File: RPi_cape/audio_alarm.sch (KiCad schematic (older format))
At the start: 70 parts, among them J13 Conn_01x02, J14 Conn_01x02, Q11 MMBT3904, Q12 MMBT3906, Q13 MMBT3904, Q5 MMBT3904, Q6 DNP, Q7 DNP, Q8 MMBT3904, U24 TL431A, U25 LM2903, U26 MIC1557, U27 MIC1557, U28 LM4871M

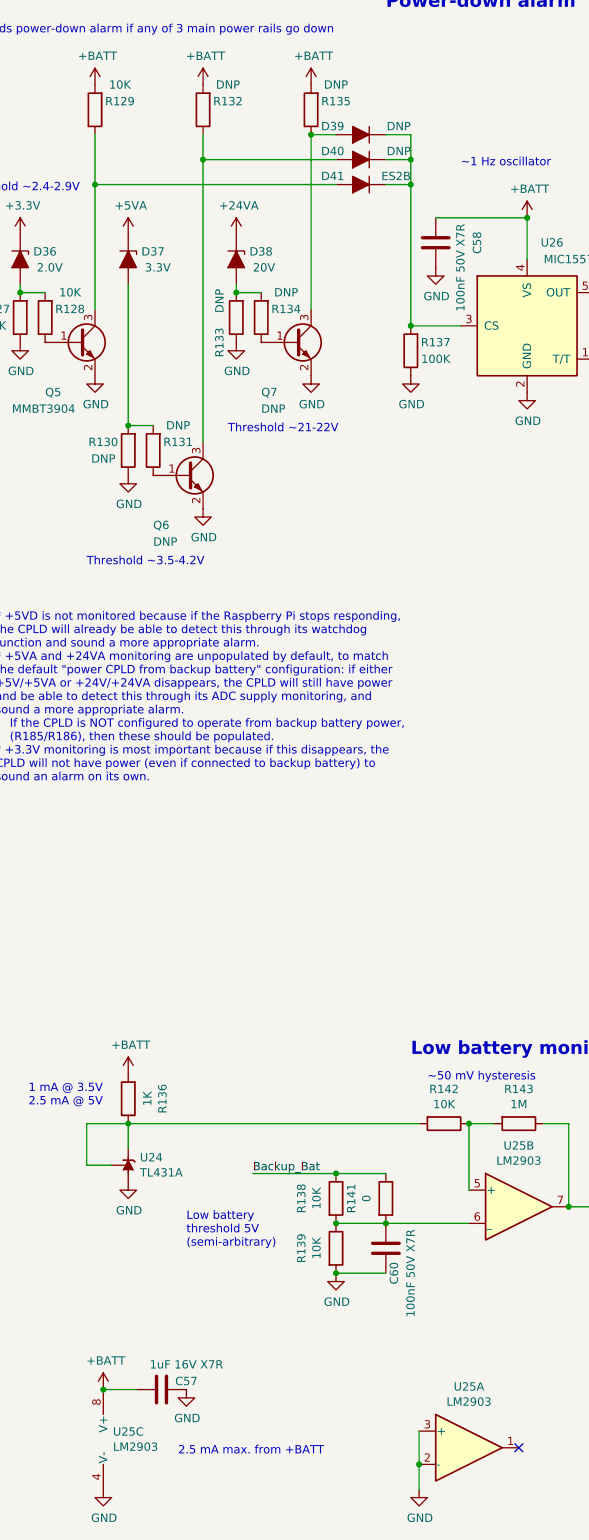
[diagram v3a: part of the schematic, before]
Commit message: Better valve monitoring, finalized layout and manufacturing files
Created assembly and fabrication drawings, assigned all BOM parts, generally made design ready for ordering
Added strain-relief slots and barb mounting dimensions for digital pressure sensors
Changed valve drivers from discrete power MOSFETs to "smart" industrial/automotive driver ICs for the current monitoring, including valve-movement monitor for #4
Connected RPi_Valve* signals to larger CPLD footprint, changed Raspberry Pi pin assignment as a result to ease PCB routing
Updated footprints, page layout to create readable assembly drawing
Added current-measurement testpoints for CPLD power from BATT+
Changed power diodes in power-down-alarm circuit to small-signal parts for more compact layout
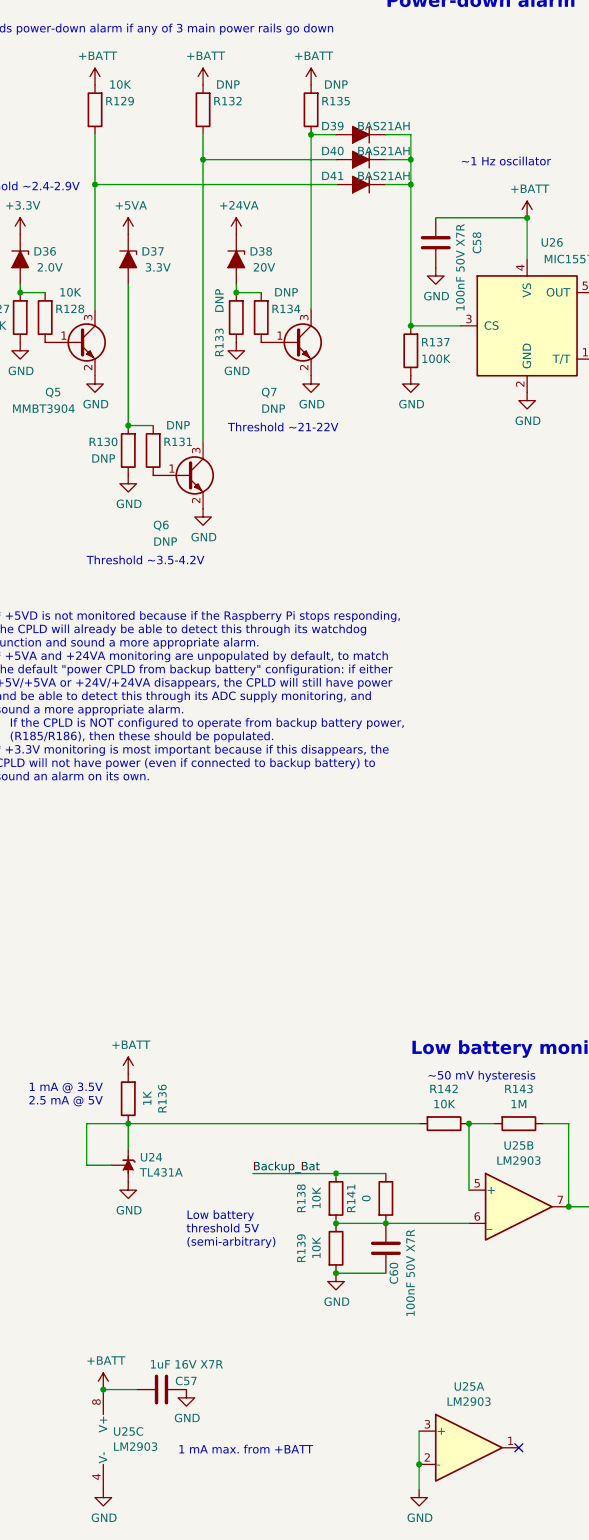
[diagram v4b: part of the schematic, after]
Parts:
- D36: footprint Diode_SMD:D_SOD-123 -> Ventilator:D_SOD-123; Manufacturer (none) -> ON Semiconductor; Part Number (none) -> MMSZ4679T1G
- D37, D52: footprint Diode_SMD:D_SOD-123 -> Ventilator:D_SOD-123; Manufacturer (none) -> ON Semiconductor; Part Number (none) -> MMSZ4684T1G
- D38: footprint Diode_SMD:D_SOD-123 -> Ventilator:D_SOD-123; Manufacturer (none) -> ON Semiconductor; Part Number (none) -> MMSZ4707T1G
- D39, D40: value DNP -> BAS21AH; footprint Diode_SMD:D_SMA -> Ventilator:D_SOD-323; Manufacturer Vishay -> ON Semiconductor; Part Number ES2G-E3/52T -> BAS21AHT1G
- D41: value ES2B -> BAS21AH; footprint Diode_SMD:D_SMA -> Ventilator:D_SOD-323; Manufacturer Vishay -> ON Semiconductor; Part Number ES2G-E3/52T -> BAS21AHT1G
- D42, D43: footprint Diode_SMD:D_SMA -> Ventilator:D_SMA
- Q11, Q13, Q5, Q8: footprint Package_TO_SOT_SMD:SOT-23 -> Ventilator:SOT-23; Manufacturer (none) -> Diodes Inc.; Part Number (none) -> MMBT3904-7-F
- Q12: footprint Package_TO_SOT_SMD:SOT-23 -> Ventilator:SOT-23; Manufacturer (none) -> Nexperia; Part Number (none) -> MMBT3906,215
- Q6, Q7, U24: footprint Package_TO_SOT_SMD:SOT-23 -> Ventilator:SOT-23
- R127, R128, R129, R138, R139, R142, R146, R148, R151, R187, R188, R191: Manufacturer (none) -> KOA Speer; Part Number (none) -> RK73H2BTTD1002F
- R136, R147: Manufacturer (none) -> KOA Speer; Part Number (none) -> RK73H2BTTD1001F
- R137, R149, R150: Manufacturer (none) -> KOA Speer; Part Number (none) -> RK73H2BTTD1003F
- R140, R143: Manufacturer (none) -> KOA Speer; Part Number (none) -> RK73H2BTTD1004F
- R141, R177, R178: Manufacturer (none) -> Panasonic; Part Number (none) -> ERJ-8GEY0R00V
- R144: Manufacturer (none) -> KOA Speer; Part Number (none) -> RK73H2BTTD2703F
- R190: Manufacturer (none) -> KOA Speer; Part Number (none) -> RK73H2BTTD3001F
- U25: footprint Package_SO:VSSOP-8_3.0x3.0mm_P0.65mm -> Ventilator:VSSOP-8_3.0x3.0mm_P0.65mm
- U26, U27: footprint Package_TO_SOT_SMD:SOT-23-5 -> Ventilator:SOT-23-5
- U28: footprint Package_SO:SOIC-8_3.9x4.9mm_P1.27mm -> Ventilator:SOIC-8_3.9x4.9mm_P1.27mm
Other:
- note added: "1 mA max. from +BATT"
- note removed: "2.5 mA max. from +BATT"

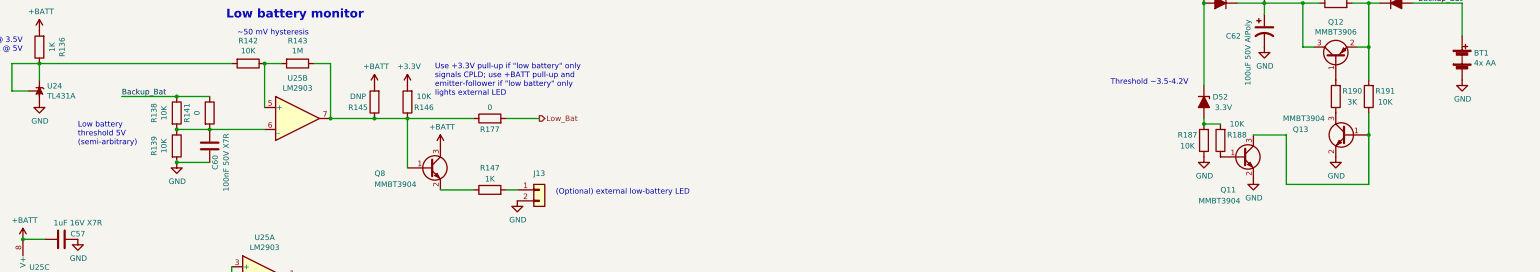
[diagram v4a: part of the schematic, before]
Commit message: Manufacturing clean-up
Corrections and additions to BOM etc. for manufacturing
Added power draw tracking spreadsheet
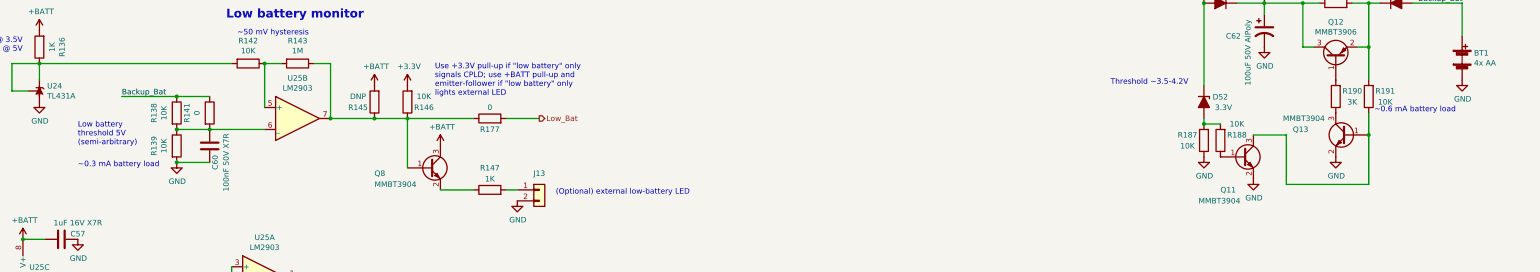
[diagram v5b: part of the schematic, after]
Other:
- note added: "~~0.3 mA battery load"
- note added: "~~0.6 mA battery load"
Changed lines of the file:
@@
 	1    0    0    -1
 $EndComp
+Text Notes 13650 8000 0    50   ~ 0
+~~0.6 mA battery load
+Text Notes 1850 8500 0    50   ~ 0
+~~0.3 mA battery load
 $EndSCHEMATC

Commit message: Safety additions
Switched CPLD_ADC7 to +24V monitoring (from +5V monitoring), and added CPLD ~Bat_On digital input(s) to know when it's running from backup battery, to cover low-input-voltage edge cases
Added series 1K resistors (R226-231) on CPLD<->RPi Comms1-6 lines, to protect CPLD in case of overvoltage from RPi failure
Added optional input TVS D23 to handle sustained over-voltage or large surges
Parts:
- added D14, D22: BAS21AH, Ventilator:D_SOD-323, symbol Device:D_ALT
- added R224, R225: 10K, Resistor_SMD:R_1206_3216Metric, symbol Device:R
- D37: value 3.3V -> DNP (3.3V)
- D38: value 20V -> DNP (20V)
- D39: value BAS21AH -> DNP (BAS21AH)
- Q6: value DNP -> MMBT3904; Manufacturer (none) -> Diodes Inc.; Part Number (none) -> MMBT3904-7-F
- R130: value DNP -> 1K; Manufacturer (none) -> KOA Speer; Part Number (none) -> RK73H2BTTD1001F
- R131, R132: value DNP -> 10K; Manufacturer (none) -> KOA Speer; Part Number (none) -> RK73H2BTTD1002F
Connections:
- net +3V3: now also R225.2
- net at Q12.1 (B), R190.2: now also R224.1
- net at D43.1 (K), Q12.2 (E), R189.2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: now also R224.2
- net at Q13.3 (C), R190.1: now also D22.1 (K)
- net at D37.2 (A), R130.2, R131.2: now also D14.1 (K)
- new net +1V8: D14.2 (A)
- new net ~Bat_On: D22.2 (A), R225.1
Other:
- note added: "Can monitor either +5VA or +1.8V,\ndepending on which diode is populated\n+5VA: threshold ~~3.5-4.2V, R130=10K (for 50uA Izener nom.)\n+1.8V: threshold ~~0.9-1.4V, R130=1K (for 0.5mA Idiode nom.)"
- note added: "Signal to CPLD, goes low when\nrunning from backup battery\npower"
- moved on the sheet: BT1, D43, R191

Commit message: Docs cleanup
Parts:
- C65: Part Number GCM32EC71H106KA03 -> GCM32EC71H106KA03L
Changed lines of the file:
@@
 F 3 "~" H 7700 1500 50  0001 C CNN
 F 4 "Murata" H 7700 1500 50  0001 C CNN "Manufacturer"
-F 5 "GCM32EC71H106KA03" H 7700 1500 50  0001 C CNN "Part Number"
+F 5 "GCM32EC71H106KA03L" H 7700 1500 50  0001 C CNN "Part Number"
 	1    7700 1500
 	-1   0    0    -1

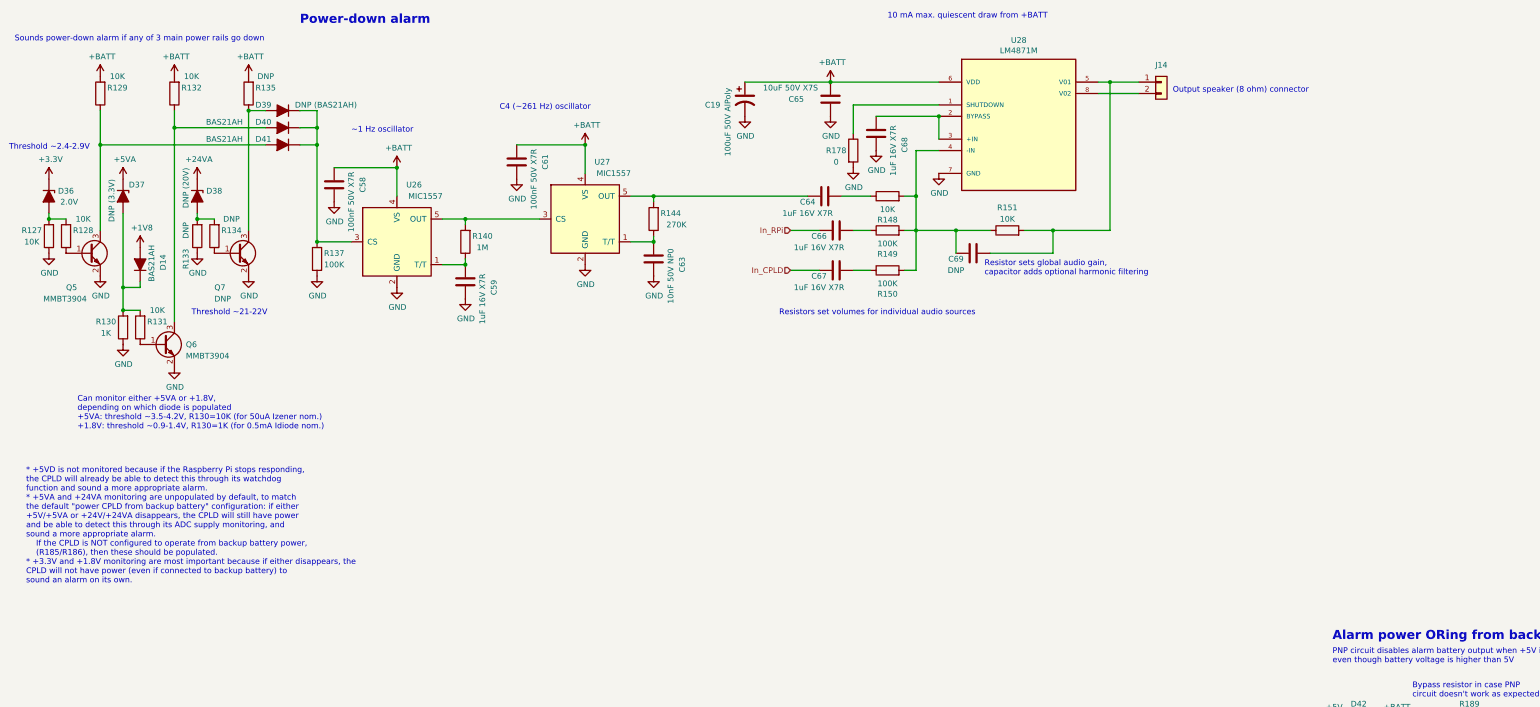
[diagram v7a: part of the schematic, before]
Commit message: +5VA outage detection
Separated +1.8V and +5VA monitoring and added +3.3V output for +5VA on ~5VA_On signal to CPLD, to cover an extra failure mode
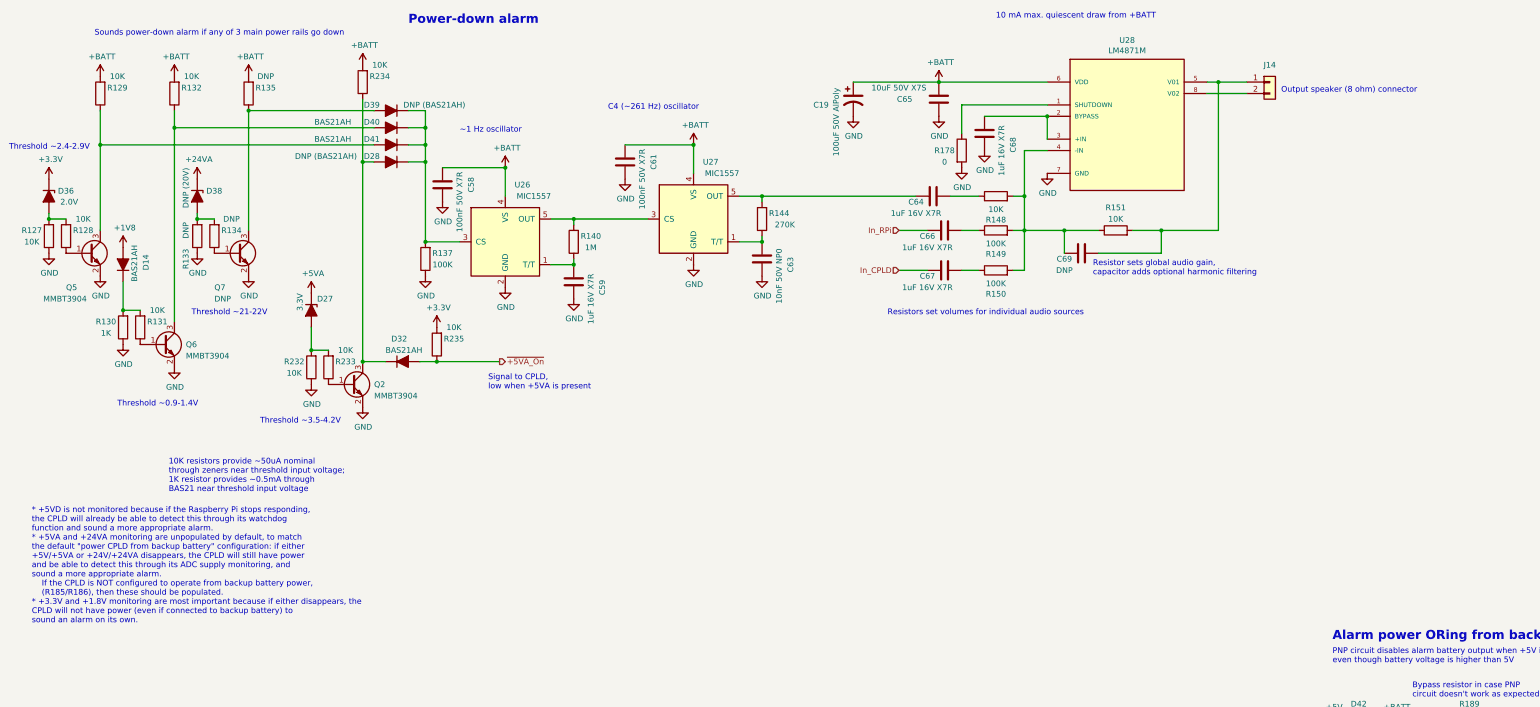
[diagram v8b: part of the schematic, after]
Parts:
- removed D37: DNP (3.3V), Ventilator:D_SOD-123, symbol Device:D_Zener_ALT
- added D27: 3.3V, Ventilator:D_SOD-123, symbol Device:D_Zener_ALT
- added D28: DNP (BAS21AH), Ventilator:D_SOD-323, symbol Device:D_ALT
- added D32: BAS21AH, Ventilator:D_SOD-323, symbol Device:D_ALT
- added Q2: MMBT3904, Ventilator:SOT-23, symbol Transistor_BJT:MMBT3904
- added R232, R233, R234, R235: 10K, Resistor_SMD:R_1206_3216Metric, symbol Device:R
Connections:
- net +3V3: now also R235.2
- net +5VA: now also D27.1 (K)
- net +BATT: now also R234.2
- net GND: now also Q2.2 (E), R232.1
- net at D39.1 (K), D40.1 (K), D41.1 (K)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: now also D28.1 (K)
- new net: D27.2 (A), R232.2, R233.2
- new net: Q2.1 (B), R233.1
- new net: D28.2 (A), D32.1 (K), Q2.3 (C), R234.1
- new net ~+5VA_On: D32.2 (A), R235.1
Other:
- note added: "10K resistors provide ~~50uA nominal\nthrough zeners near threshold input voltage;\n1K resistor provides ~~0.5mA through\nBAS21 near threshold input voltage"
- note added: "Signal to CPLD,\nlow when +5VA is present"
- note added: "Threshold ~~0.9-1.4V"
- note removed: "Can monitor either +5VA or +1.8V,\ndepending on which diode is populated\n+5VA: threshold ~~3.5-4.2V, R130=10K (for 50uA Izener nom.)\n+1.8V: threshold ~~0.9-1.4V, R130=1K (for 0.5mA Idiode nom.)"
- moved on the sheet: C19, C58, C59, C61, C63, C64, C65, C66, C67, C68, C69, D14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
